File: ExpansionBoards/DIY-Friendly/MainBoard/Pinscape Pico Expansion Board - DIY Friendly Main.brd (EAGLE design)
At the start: 160 x 107 mm, 115 parts, among them IC1 UCC27524P, IC10 ULN2803A, IC11 SN74HC165N, IC12 SN74HC165N, IC13 SN74HC74NE4, IC14 PC827, IC15 S-80833CLY, IC16 SN74HC165N, IC18 SN74HC165N, IC2 UCC27524P, IC3 UCC27524P, IC4 UCC27524P, IC5 UCC27524P, IC6 UCC27524P, IC7 ULN2803A, IC8 ULN2803A, IC9 ULN2803A, J1 30316-6002HB, J10 215079-4, J11 640454-2, J13 640445-2, J14 SSQ-108-02-T-S-RA, J2 640445-6, J3 640445-5, J4 640445-9, J5 1-640456-0, J6 1-640456-0, J7 1-640456-0, J8 1-640456-0, J9 30308-6002HB, Q1 FDPF085N10A, Q10 FDPF085N10A, Q11 FDPF085N10A, Q12 FDPF085N10A, Q13 BC337-25, Q15 2N5195G, Q16 2N2222A, Q2 FDPF085N10A, Q3 FDPF085N10A, Q4 FDPF085N10A, Q5 FDPF085N10A, Q6 FDPF085N10A, Q7 FDPF085N10A, Q8 FDPF085N10A, Q9 FDPF085N10A

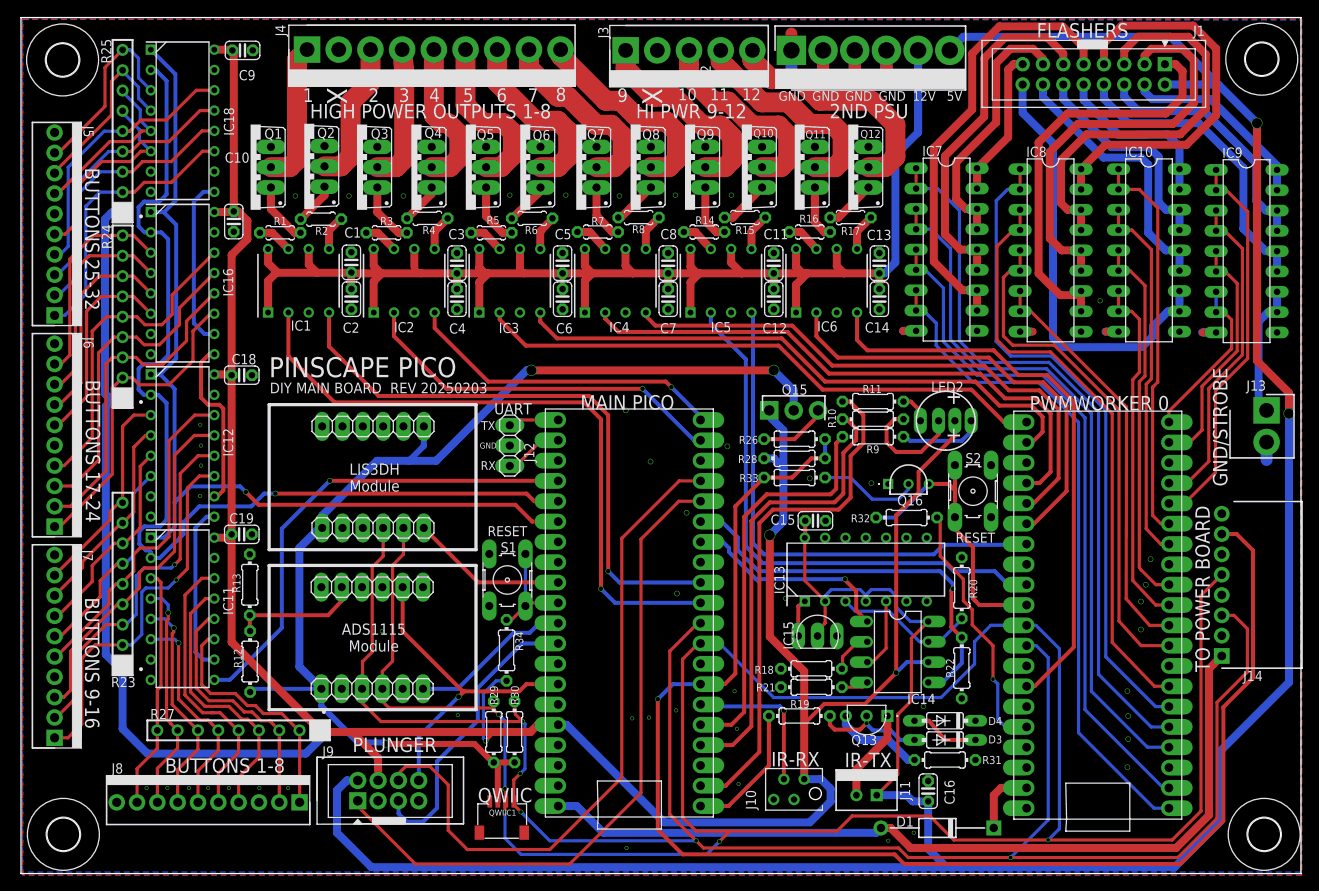
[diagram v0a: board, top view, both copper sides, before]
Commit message: PCB parts lists (BOMs); power distro board edits
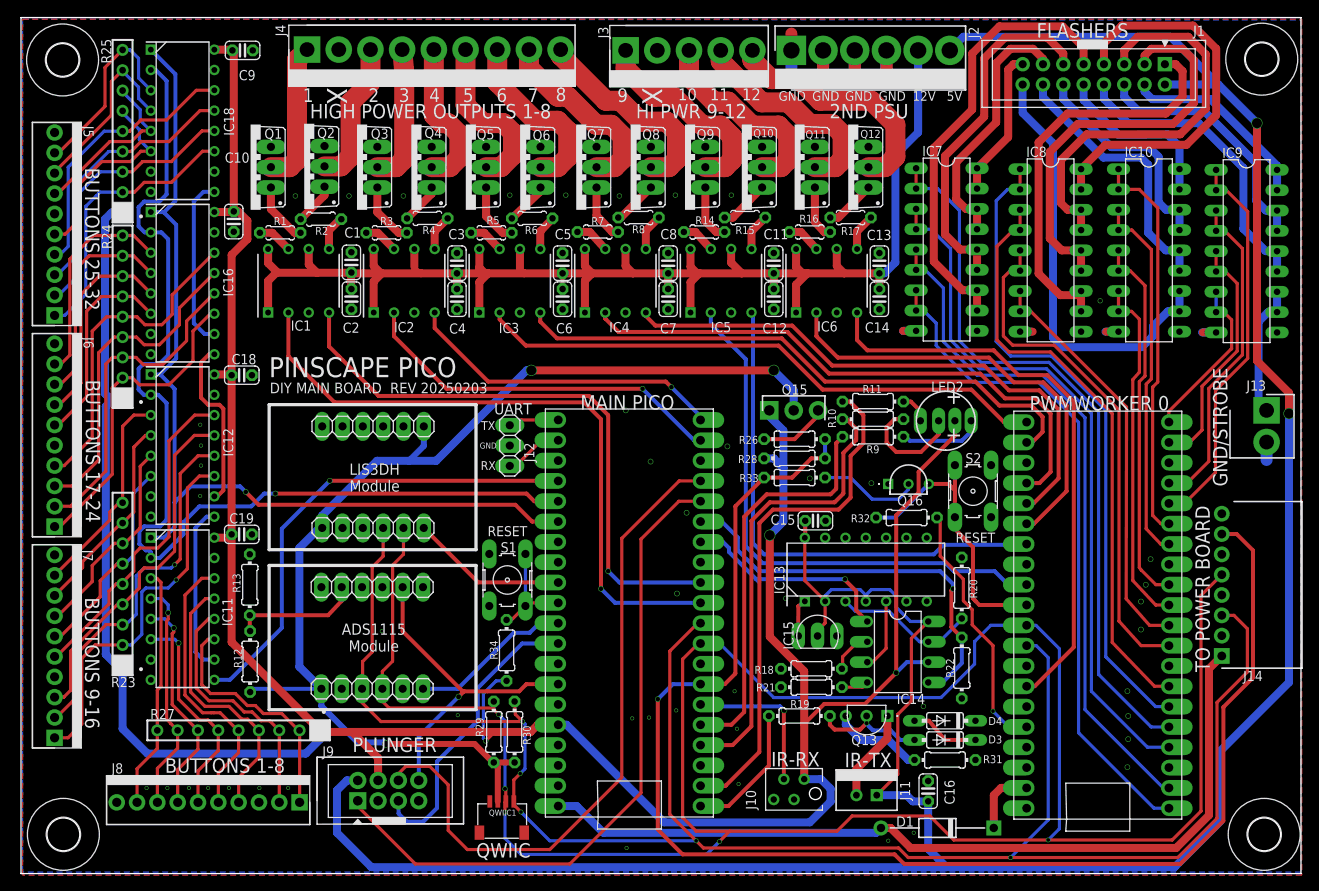
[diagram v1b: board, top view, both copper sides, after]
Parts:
- S1, S2: value (none) -> B3F-1000

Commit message: BOM tweaks
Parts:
- Q1, Q10, Q11, Q12, Q3, Q4, Q5, Q6, Q7, Q8, Q9: value FDPF085N10A -> STP19NF20
- R1, R14, R15, R16, R17, R2, R3, R4, R5, R6, R7, R8: value 4R7 -> 200R

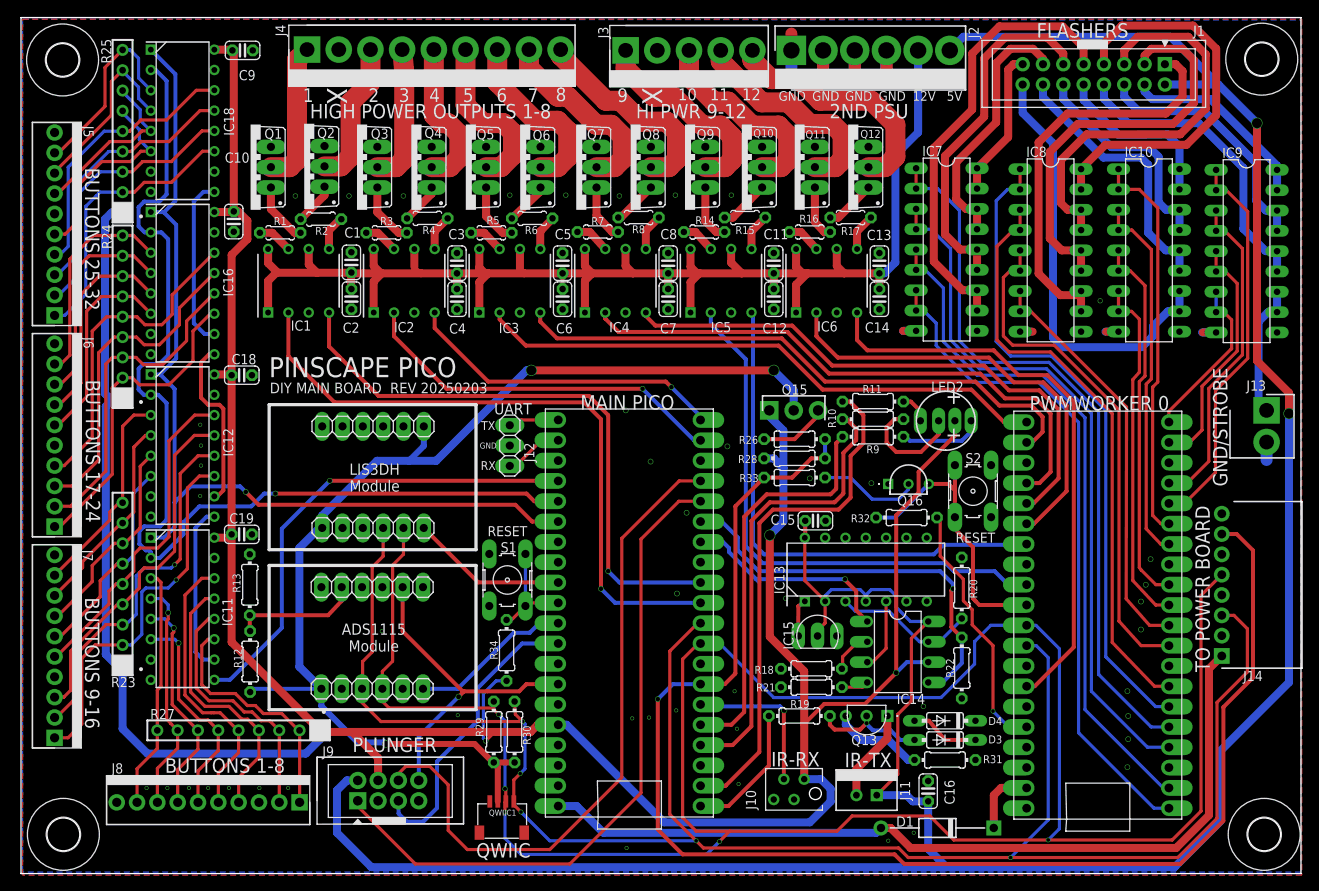
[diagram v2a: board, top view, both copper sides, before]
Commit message: exp board: DIY main: move main Pico reset switch to a more accessible spot
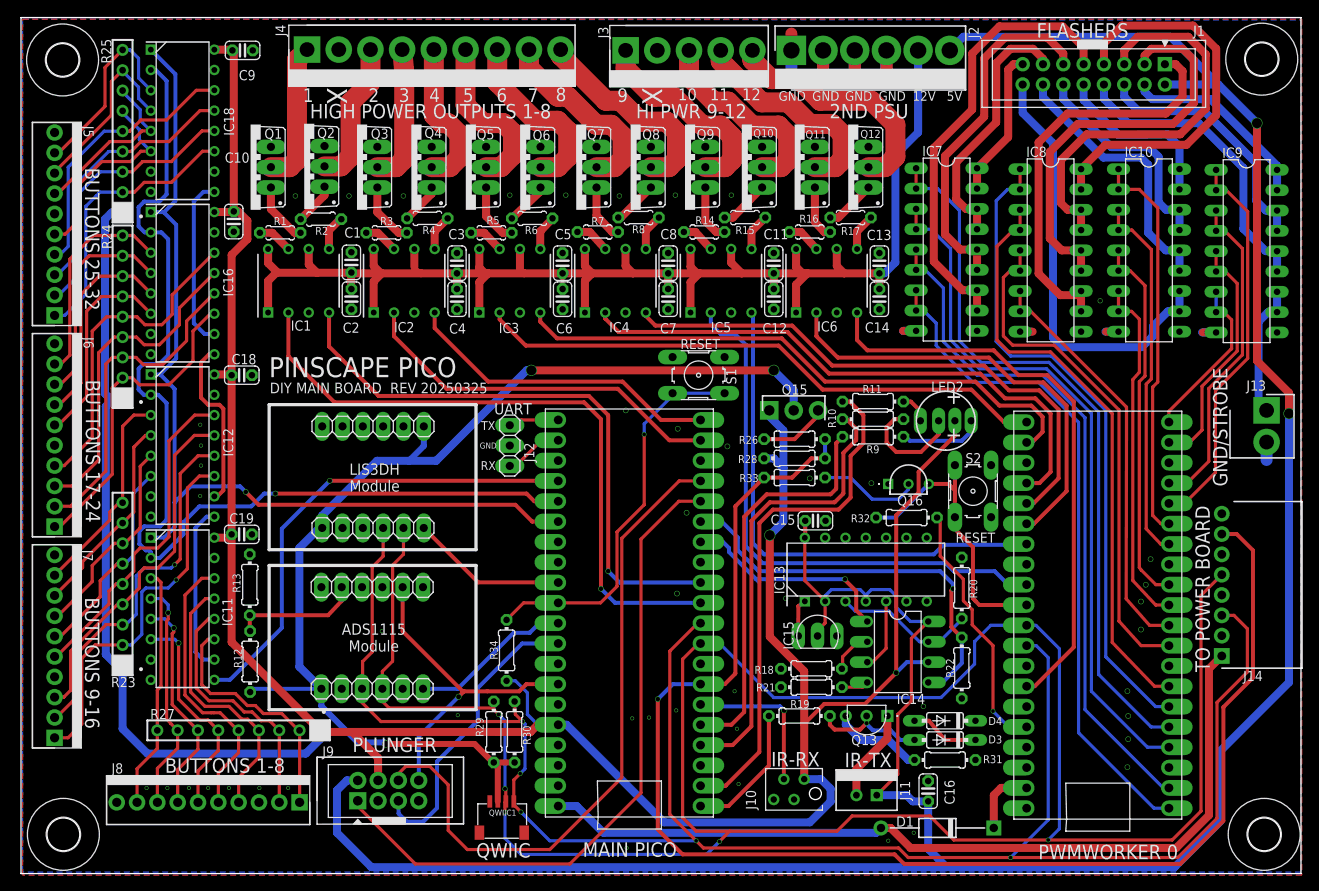
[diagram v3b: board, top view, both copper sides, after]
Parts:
- moved S1 35.0 mm to (84.7, 57.3), turned to 0 degrees
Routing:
- net N$36: track 13.8 -> 49.1 mm, vias 0 -> 1
- net OUTCTL9: track 68.1 -> 69.2 mm
- net 3V3_PICO: track 398.8 -> 398.0 mm, vias 3 -> 2
- net OUTCTL4: track 40.2 -> 39.9 mm, vias 1 -> 0
- net OUTCTL3: vias 1 -> 0
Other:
- board text added: "DIY MAIN BOARD REV 20250325"
- board text removed: "DIY MAIN BOARD REV 20250203"

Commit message: exp board: DIY: add errata to readme; reorient main board Flasher header silkscreen markings to match KL25Z expansion boards
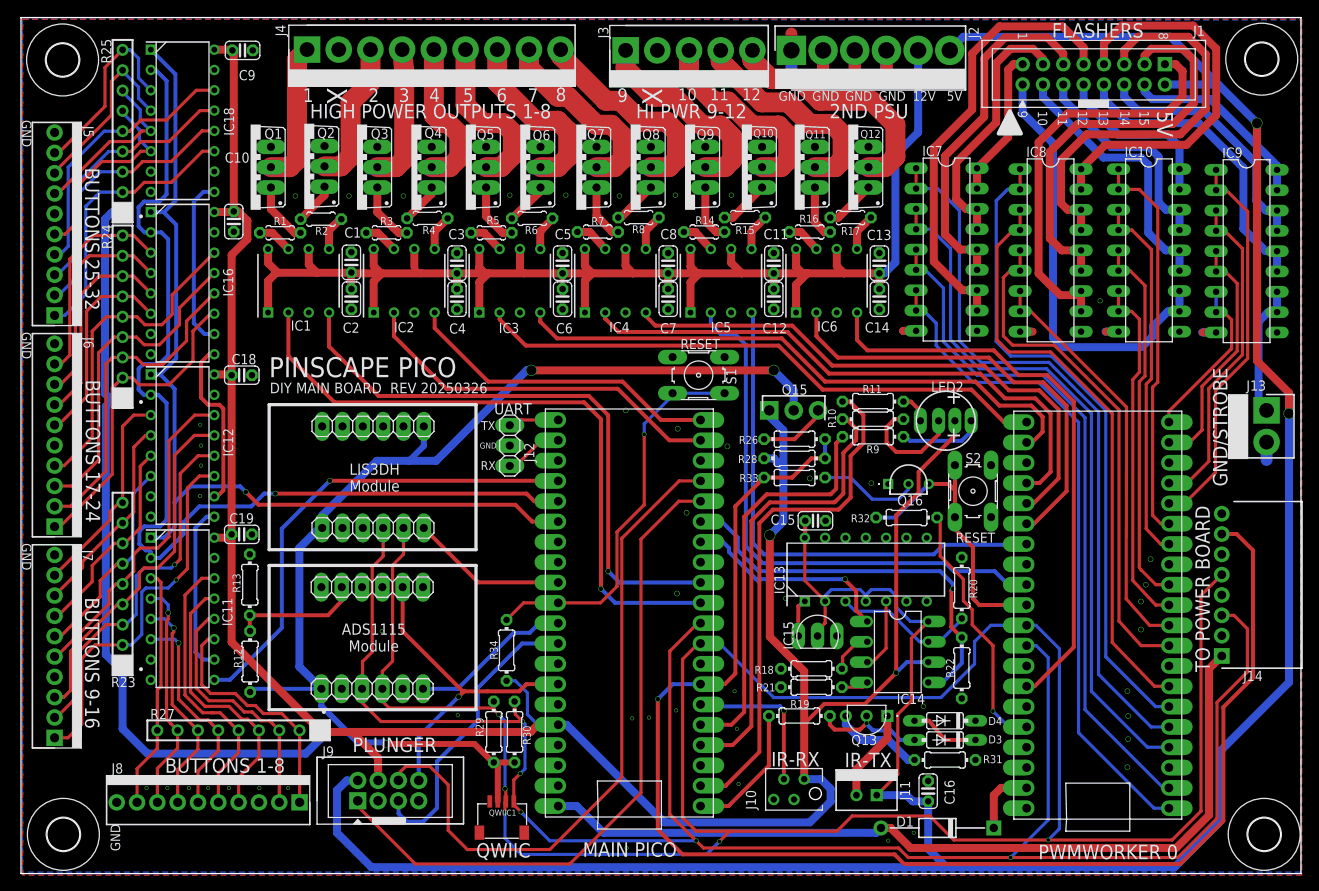
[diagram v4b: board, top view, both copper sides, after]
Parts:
- J1: value 30316-6002HB -> 30316-6002HBROTATED; device SamacSys_Parts:3M-30316-6002HB -> SamacSys_Parts:3M-30316-6002HB-ROTATED
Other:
- board text added: "13"
- board text added: "14"
- board text added: "15"
- board text added: "DIY MAIN BOARD REV 20250326"
- board text removed: "DIY MAIN BOARD REV 20250325"
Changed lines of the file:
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@@
 <wire x1="31.02" y1="35.484" x2="31.02" y2="53.616" width="0.4064" layer="21"/>
 <text x="31" y="58.3" size="2.5" layer="25" ratio="15" rot="SR0" align="center-left">PINSCAPE PICO</text>
-<text x="31.1" y="55.7" size="1.33" layer="25" ratio="20" rot="SR0" align="center-left">DIY MAIN BOARD  REV 20250325</text>
+<text x="31.1" y="55.7" size="1.33" layer="25" ratio="20" rot="SR0" align="center-left">DIY MAIN BOARD  REV 20250326</text>
 <text x="46.7" y="11.1" size="1.8" layer="25" ratio="15" rot="SR0" align="center">PLUNGER</text>
 <text x="25.5" y="8.5" size="1.8" layer="25" ratio="15" rot="SR0" align="center">BUTTONS 1-8</text>
@@
 <text x="39.5" y="92.2" size="2.5" layer="25" ratio="15" rot="SR270" align="center">X</text>
 <text x="116.6" y="49.9" size="2" layer="25" ratio="20" rot="SR0" align="center">+</text>
-<text x="132.7" y="100.4" size="1.8" layer="25" ratio="15" rot="SR0" align="center">FLASHERS</text>
+<text x="134.6" y="100.4" size="1.8" layer="25" ratio="15" rot="SR0" align="center">FLASHERS</text>
 <text x="61.5" y="53.1" size="1.4" layer="21" ratio="15" align="center">UART</text>
 <text x="58.4" y="51" size="1.1" layer="21" ratio="15" align="center">TX</text>
@@
 <text x="96.4" y="92.2" size="1.2" layer="25" ratio="15" rot="SR0" align="center">GND</text>
 <text x="119.3" y="37" size="1.25" layer="21" ratio="15" align="center">RESET</text>
+<text x="143" y="88.7" size="2" layer="25" ratio="15" rot="SR270" align="center">5V</text>
+<text x="140.4" y="89.4" size="1.2" layer="25" ratio="15" rot="SR270" align="center">15</text>
+<text x="138" y="89.4" size="1.2" layer="25" ratio="15" rot="SR270" align="center">14</text>
+<text x="135.3" y="89.4" size="1.2" layer="25" ratio="15" rot="SR270" align="center">13</text>
+<text x="132.7" y="89.4" size="1.2" layer="25" ratio="15" rot="SR270" align="center">12</text>
+<text x="130.2" y="89.4" size="1.2" layer="25" ratio="15" rot="SR270" align="center">11</text>
+<text x="127.7" y="89.4" size="1.2" layer="25" ratio="15" rot="SR270" align="center">10</text>
+<text x="125.2" y="89.9" size="1.2" layer="25" ratio="15" rot="SR270" align="center">9</text>
+<text x="142.8" y="99.7" size="1.2" layer="25" ratio="15" rot="SR270" align="center">8</text>
+<text x="125.2" y="99.7" size="1.2" layer="25" ratio="15" rot="SR270" align="center">1</text>
+<polygon width="0.5" layer="21">
+<vertex x="122.2" y="87.5"/>
+<vertex x="123.6" y="90.3"/>
+<vertex x="125" y="87.5"/>
+</polygon>
+<text x="11.8" y="-0.5" size="1.2" layer="25" ratio="15" rot="SR90" align="center">GND</text>
+<text x="0.7" y="34.6" size="1.2" layer="25" ratio="15" rot="SR270" align="center">GND</text>
+<text x="0.7" y="61" size="1.2" layer="25" ratio="15" rot="SR270" align="center">GND</text>
+<text x="0.7" y="87.5" size="1.2" layer="25" ratio="15" rot="SR270" align="center">GND</text>
 </plain>
 <attributes>
@@
 <element name="IC9" library="uln-udn" package="DIL18" value="ULN2803A" x="153.2" y="72.8" rot="R270"/>
 <element name="IC10" library="uln-udn" package="DIL18" value="ULN2803A" x="141" y="72.9" rot="R270"/>
-<element name="J1" library="SamacSys_Parts" package="3M-30316-6002HB" value="30316-6002HB" x="134.1" y="94.9" smashed="yes" rot="R180">
-<attribute name="MOUSER_PRICE-STOCK" value="https://www.mouser.co.uk/ProductDetail/3M-Electronic-Solutions-Division/30316-6002HB?qs=QV10cN0MjFtE79zTqp0XZw%3D%3D" x="134.1" y="94.9" size="0.6" layer="27" rot="R180" display="off"/>
-<attribute name="HEIGHT" value="mm" x="134.1" y="94.9" size="0.6" layer="27" rot="R180" display="off"/>
-<attribute name="MANUFACTURER_PART_NUMBER" value="30316-6002HB" x="134.1" y="94.9" size="0.6" layer="27" rot="R180" display="off"/>
-<attribute name="MANUFACTURER_NAME" value="3M" x="134.1" y="94.9" size="0.6" layer="27" rot="R180" display="off"/>
-<attribute name="MOUSER_PART_NUMBER" value="517-30316-6002" x="134.1" y="94.9" size="0.6" layer="27" rot="R180" display="off"/>
-<attribute name="DESCRIPTION" value="Low Profile Header" x="134.1" y="94.9" size="0.6" layer="27" rot="R180" display="off"/>
+<element name="J1" library="SamacSys_Parts" package="3M-30316-6002HB-ROTATED" value="30316-6002HBROTATED" x="134.1" y="94.9" smashed="yes" rot="R180">
 <attribute name="VALUE" x="134.1" y="91.2805" size="0.7" layer="27" rot="R180" align="center"/>
 <attribute name="NAME" x="147.2505" y="100.347" size="1.27" layer="25" rot="R180" align="center"/>

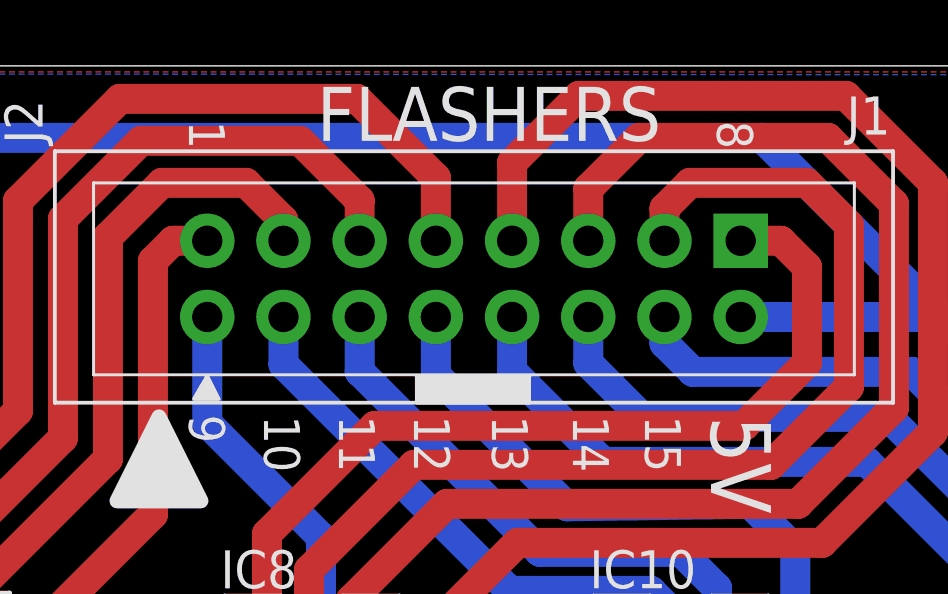
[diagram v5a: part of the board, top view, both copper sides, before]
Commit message: exp board: power distribution: 24-pin ATX connector, 48V interlock via MOSFET, Always On jumper options
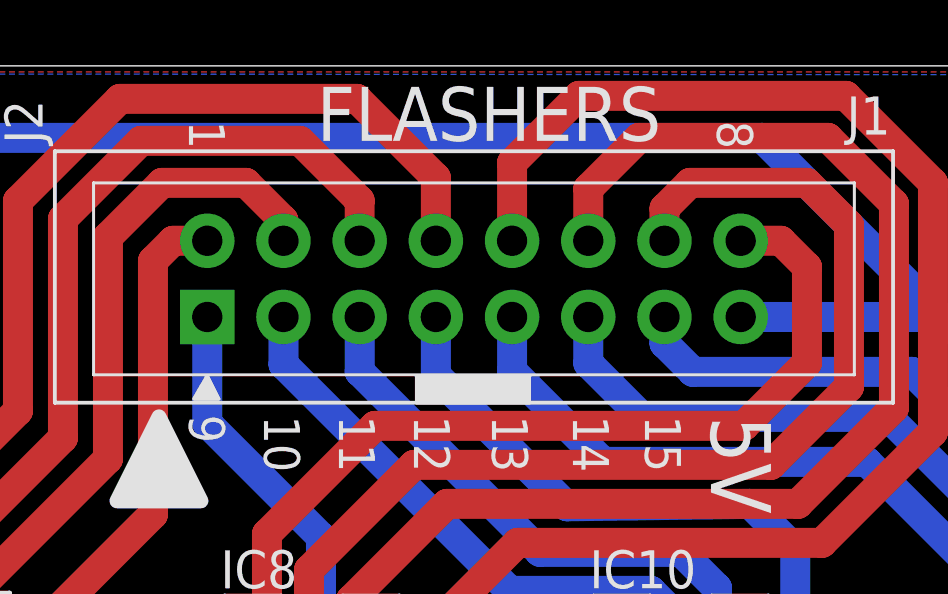
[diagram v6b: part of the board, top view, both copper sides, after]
